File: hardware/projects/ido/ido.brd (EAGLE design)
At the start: 48.3 x 48.3 mm, 36 parts, among them U1 PADI-IOT-STAMP, U2 POLOLU-BUCK, U3 AL8805W5, U4 AL8805W5, U5 AL8805W5, X1 PROGRAMMING-HEADER, X10 WIRE-HOLE, X2 UART-HEADER, X3 WIRE-HOLE, X4 WIRE-HOLE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

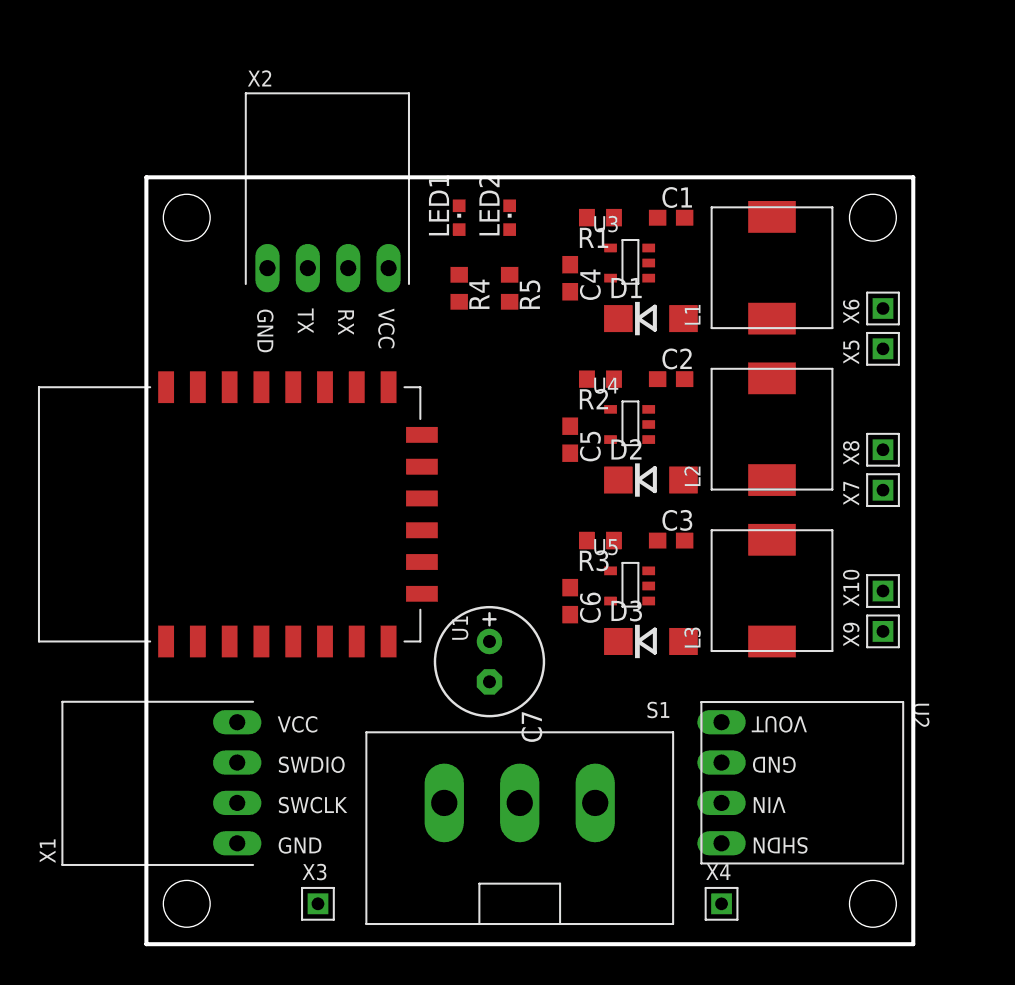
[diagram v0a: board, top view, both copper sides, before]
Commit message: Board and hole dimensions set and layout WIP.
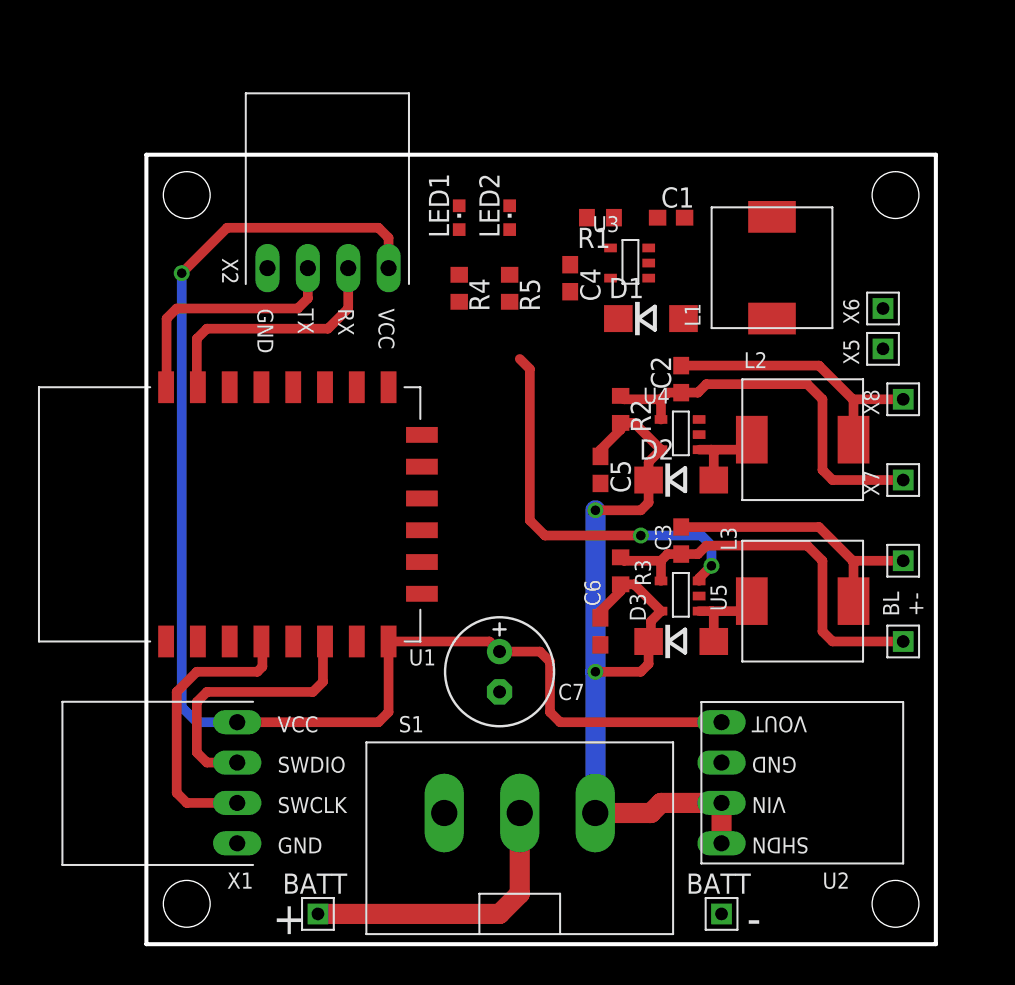
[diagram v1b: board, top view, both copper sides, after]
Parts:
- moved X8 3.42 mm to (47.6, 34.3)
- moved U5 3.24 mm to (32.4, 22.9)
- moved U4 3.24 mm to (32.4, 33.0)
- moved L2 2.84 mm to (38.1, 31.8), turned to 0 degrees
- moved L3 2.84 mm to (38.1, 21.6), turned to 0 degrees
- moved C5 2.69 mm to (28.6, 29.8)
- moved C6 2.69 mm to (28.6, 19.7)
- moved R2 2.29 mm to (29.8, 33.7), turned to 270 degrees
- moved X10 2.29 mm to (47.6, 24.1)
- moved R3 2.29 mm to (29.8, 23.5), turned to 270 degrees
- moved D2 1.91 mm to (33.7, 29.2)
- moved D3 1.91 mm to (33.7, 19.1)
- moved X7 1.42 mm to (47.6, 29.2)
- moved X9 1.42 mm to (47.6, 19.1)
- moved C7 0.90 mm to (22.2, 17.1)
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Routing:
- net +3V3: track 0.00 -> 86.7 mm, vias 0 -> 1
- net V+: track 0.00 -> 56.0 mm, vias 0 -> 2
- net BCTRL: track 0.00 -> 25.1 mm, vias 0 -> 2
- net G+: track 0.00 -> 24.6 mm
- net B+: track 0.00 -> 24.6 mm
- net N$1: track 0.00 -> 18.3 mm
- net SWCLK: track 0.00 -> 18.1 mm
- net B-: track 0.00 -> 17.4 mm
- net G-: track 0.00 -> 17.4 mm
- net SWDIO: track 0.00 -> 17.0 mm
- net RX: track 0.00 -> 15.9 mm
- net TX: track 0.00 -> 15.7 mm
- net N$9: track 0.00 -> 5.55 mm
- net N$6: track 0.00 -> 5.55 mm
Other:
- board size 48.3 x 48.3 mm -> 49.7 x 49.7 mm
- board text added: "+"
- board text added: "-"
- board text added: "BATT"
- board text added: "BL +-"

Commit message: Final board rev.
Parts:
- moved X3 39.8 mm to (49.8, 9.53), turned to 90 degrees
- moved X4 17.8 mm to (49.8, 13.3), turned to 90 degrees
- moved LED2 14.0 mm to (21.6, 31.8), turned to 270 degrees
- moved R5 12.8 mm to (21.6, 28.6), turned to 0 degrees
- moved X2 12.7 mm to (19.7, 46.4)
- moved LED1 8.16 mm to (21.6, 37.8), turned to 270 degrees
- moved R4 6.93 mm to (21.6, 34.6), turned to 0 degrees
- moved U1 5.71 mm to (15.2, 24.8)
- moved U2 5.68 mm to (41.3, 11.4), turned to 180 degrees
- moved U3 5.12 mm to (33.7, 41.3)
- moved C4 4.96 mm to (29.8, 38.1)
- moved R1 4.58 mm to (31.1, 41.9), turned to 270 degrees
- moved X1 4.45 mm to (5.71, 10.8)
- moved X6 3.98 mm to (49.8, 41.9)
- moved D1 3.70 mm to (34.9, 37.5)
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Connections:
- removed net N$2: LED1.A, R4.1
- new net N$5: LED1.C, R4.2
- net DEBUG1: now also LED1.A; no longer R4.2
- net DEBUG2: now also LED2.A; no longer R5.2
- net GND: now also R4.1, R5.1; no longer LED1.C, LED2.C
- net N$3: now also LED2.C, R5.2; no longer LED2.A, R5.1
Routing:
- net RCTRL: track 0.00 -> 42.5 mm, vias 0 -> 2
- net GCTRL: track 0.00 -> 42.2 mm, vias 0 -> 2
- net R+: track 0.00 -> 25.9 mm
- net V+: track 56.0 -> 80.4 mm, vias 2 -> 3
- net BCTRL: track 25.1 -> 47.9 mm
- net R-: track 0.00 -> 18.4 mm
- net N$1: track 18.3 -> 34.8 mm
- net +3V3: track 86.7 -> 102.1 mm, vias 1 -> 0
- net RX: track 15.9 -> 27.3 mm
- net TX: track 15.7 -> 26.8 mm
- net N$4: track 0.00 -> 5.55 mm
- net DEBUG1: track 0.00 -> 3.51 mm
- net DEBUG2: track 0.00 -> 3.51 mm
- net N$3: track 0.00 -> 3.22 mm
- net N$5: track 0.00 -> 3.22 mm
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- added copper zone on layer 1, net GND
- added copper zone on layer 16, net GND
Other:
- board size 49.7 x 49.7 mm -> 52.5 x 52.5 mm
- board text added: "2017-05-19"
- board text added: "BAT"
- board text added: "BLU"
- board text added: "GRN"
- board text added: "Maria & Bob"
- board text added: "RED"
- board text added: "iDo v1.0"
- board text removed: "BATT"
- board text removed: "BL +-"

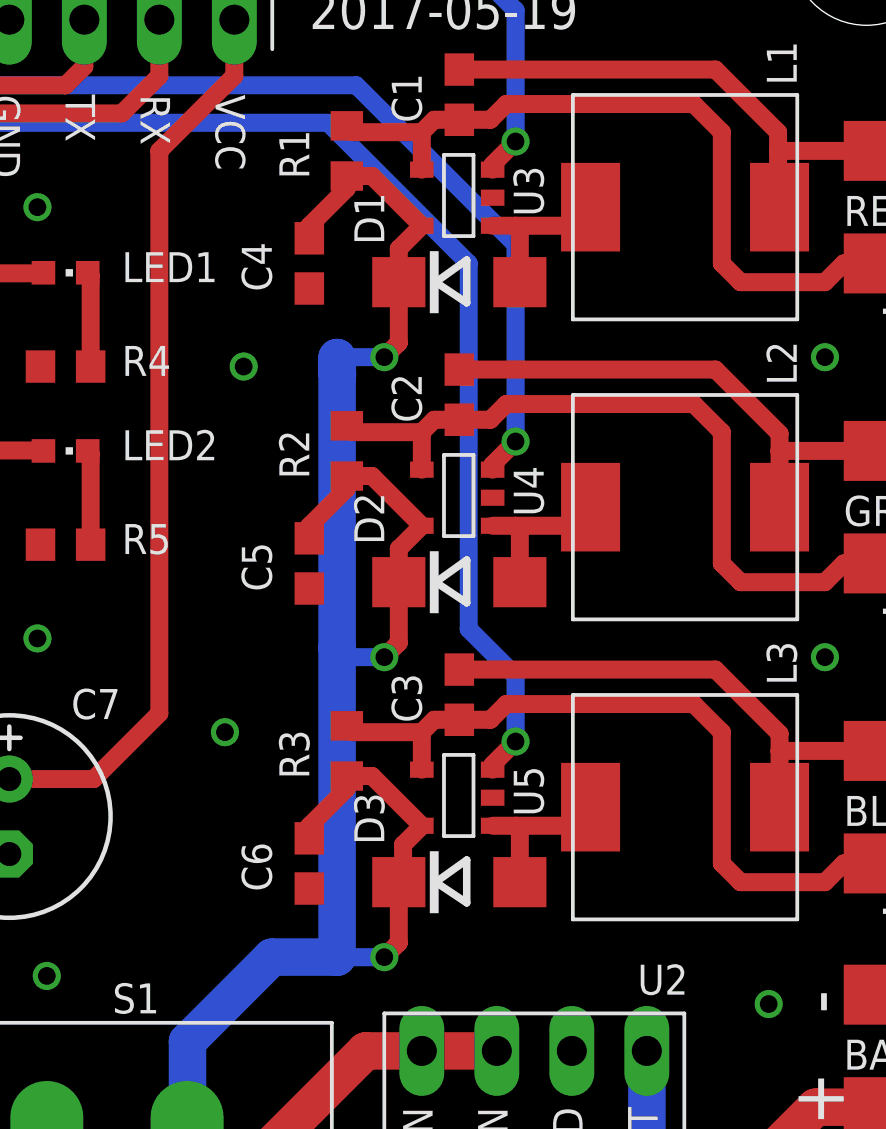
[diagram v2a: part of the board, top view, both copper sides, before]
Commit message: Move diodes down a bit to make assembly easier.
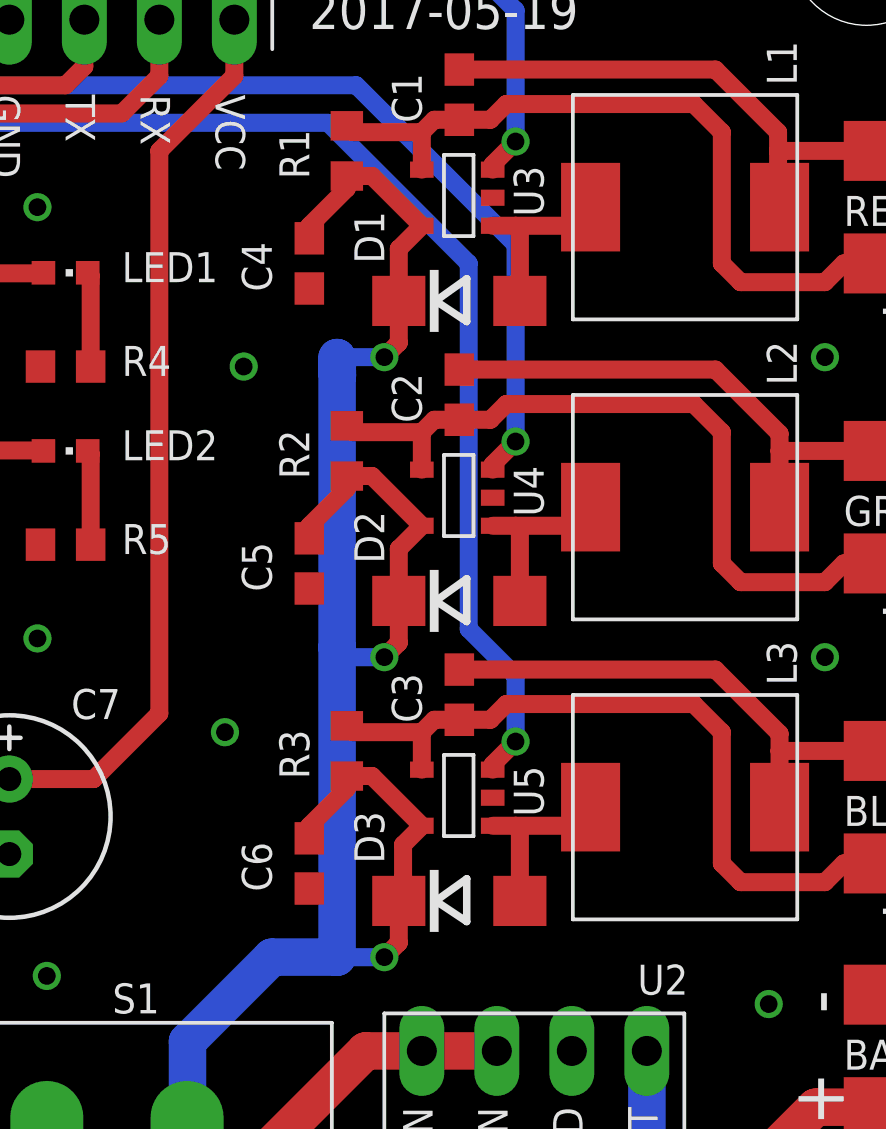
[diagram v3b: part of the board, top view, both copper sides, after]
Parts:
- moved D1 0.64 mm to (34.9, 36.8)
- moved D2 0.63 mm to (34.9, 26.7)
- moved D3 0.63 mm to (34.9, 16.5)
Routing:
- net N$4: track 5.55 -> 6.18 mm
- net N$9: track 5.55 -> 6.18 mm
- net N$6: track 5.55 -> 6.18 mm
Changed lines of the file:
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@@
 <attribute name="VALUE" x="16.51" y="16.3195" size="1.27" layer="27" ratio="10" rot="R270"/>
 </element>
-<element name="D1" library="diode" package="DO214AC" value="" x="34.925" y="37.465" smashed="yes">
-<attribute name="NAME" x="32.385" y="38.735" size="1.016" layer="25" font="vector" ratio="15" rot="R90"/>
-<attribute name="VALUE" x="32.285" y="34.909" size="1.27" layer="27" ratio="10"/>
-</element>
-<element name="D2" library="diode" package="DO214AC" value="" x="34.925" y="27.305" smashed="yes">
-<attribute name="NAME" x="32.385" y="28.575" size="1.016" layer="25" font="vector" ratio="15" rot="R90"/>
-<attribute name="VALUE" x="32.285" y="24.749" size="1.27" layer="27" ratio="10"/>
-</element>
-<element name="D3" library="diode" package="DO214AC" value="" x="34.925" y="17.145" smashed="yes">
-<attribute name="NAME" x="32.385" y="18.415" size="1.016" layer="25" font="vector" ratio="15" rot="R90"/>
-<attribute name="VALUE" x="32.285" y="14.589" size="1.27" layer="27" ratio="10"/>
+<element name="D1" library="diode" package="DO214AC" value="" x="34.925" y="36.83" smashed="yes">
+<attribute name="NAME" x="32.385" y="38.1" size="1.016" layer="25" font="vector" ratio="15" rot="R90"/>
+<attribute name="VALUE" x="32.285" y="34.274" size="1.27" layer="27" ratio="10"/>
+</element>
+<element name="D2" library="diode" package="DO214AC" value="" x="34.925" y="26.67" smashed="yes">
+<attribute name="NAME" x="32.385" y="27.94" size="1.016" layer="25" font="vector" ratio="15" rot="R90"/>
+<attribute name="VALUE" x="32.285" y="24.114" size="1.27" layer="27" ratio="10"/>
+</element>
+<element name="D3" library="diode" package="DO214AC" value="" x="34.925" y="16.51" smashed="yes">
+<attribute name="NAME" x="32.385" y="17.78" size="1.016" layer="25" font="vector" ratio="15" rot="R90"/>
+<attribute name="VALUE" x="32.285" y="13.954" size="1.27" layer="27" ratio="10"/>
 </element>
 <element name="L1" library="ido" package="MURATA-INDUCTOR" value="33uH" x="39.37" y="40.005" smashed="yes">
@@
 <wire x1="33.655" y1="19.05" x2="33.02" y2="18.415" width="0.6096" layer="1"/>
 <wire x1="33.02" y1="18.415" x2="33.02" y2="17.29" width="0.6096" layer="1"/>
-<wire x1="33.02" y1="17.29" x2="32.875" y2="17.145" width="0.6096" layer="1"/>
+<wire x1="33.02" y1="17.29" x2="32.875" y2="16.51" width="0.6096" layer="1"/>
 <wire x1="31.115" y1="20.74" x2="31.97" y2="20.74" width="0.6096" layer="1"/>
 <wire x1="31.97" y1="20.74" x2="33.655" y2="19.055" width="0.6096" layer="1"/>
@@
 <wire x1="31.115" y1="30.9" x2="31.97" y2="30.9" width="0.6096" layer="1"/>
 <wire x1="31.97" y1="30.9" x2="33.655" y2="29.215" width="0.6096" layer="1"/>
-<wire x1="32.875" y1="27.305" x2="32.875" y2="28.435" width="0.6096" layer="1"/>
+<wire x1="32.875" y1="26.67" x2="32.875" y2="28.435" width="0.6096" layer="1"/>
 <wire x1="32.875" y1="28.435" x2="33.655" y2="29.215" width="0.6096" layer="1"/>
 <wire x1="29.845" y1="28.79" x2="29.845" y2="29.21" width="0.6096" layer="1"/>
@@
 <wire x1="31.115" y1="41.06" x2="31.97" y2="41.06" width="0.6096" layer="1"/>
 <wire x1="31.97" y1="41.06" x2="33.655" y2="39.375" width="0.6096" layer="1"/>
-<wire x1="32.875" y1="37.465" x2="32.875" y2="38.595" width="0.6096" layer="1"/>
+<wire x1="32.875" y1="36.83" x2="32.875" y2="38.595" width="0.6096" layer="1"/>
 <wire x1="32.875" y1="38.595" x2="33.655" y2="39.375" width="0.6096" layer="1"/>
 <wire x1="29.845" y1="38.95" x2="29.845" y2="39.37" width="0.6096" layer="1"/>
@@
 <wire x1="30.7848" y1="14.605" x2="30.7848" y2="25.0952" width="1.27" layer="16"/>
 <wire x1="33.655" y1="11.43" x2="36.195" y2="11.43" width="1.27" layer="1"/>
-<wire x1="32.875" y1="17.145" x2="32.875" y2="15.095" width="0.6096" layer="1"/>
+<wire x1="32.875" y1="16.51" x2="32.875" y2="15.095" width="0.6096" layer="1"/>
 <wire x1="32.875" y1="15.095" x2="32.385" y2="14.605" width="0.6096" layer="1"/>
 <via x="32.385" y="14.605" extent="1-16" drill="0.6"/>
 <wire x1="32.385" y1="14.605" x2="30.7848" y2="14.605" width="0.6096" layer="16"/>
 <wire x1="30.7848" y1="25.0952" x2="31.115" y2="24.765" width="0.6096" layer="16"/>
-<wire x1="32.875" y1="27.305" x2="32.875" y2="25.255" width="0.6096" layer="1"/>
+<wire x1="32.875" y1="26.67" x2="32.875" y2="25.255" width="0.6096" layer="1"/>
 <wire x1="32.875" y1="25.255" x2="32.385" y2="24.765" width="0.6096" layer="1"/>
 <via x="32.385" y="24.765" extent="1-16" drill="0.6"/>
 <wire x1="32.385" y1="24.765" x2="31.115" y2="24.765" width="0.6096" layer="16"/>
-<wire x1="32.875" y1="37.465" x2="32.875" y2="35.415" width="0.6096" layer="1"/>
+<wire x1="32.875" y1="36.83" x2="32.875" y2="35.415" width="0.6096" layer="1"/>
 <wire x1="32.875" y1="35.415" x2="32.385" y2="34.925" width="0.6096" layer="1"/>
 <via x="32.385" y="34.925" extent="1-16" drill="0.6"/>
@@
 <wire x1="36.83" y1="39.375" x2="38.74" y2="39.375" width="0.6096" layer="1"/>
 <wire x1="38.74" y1="39.375" x2="39.37" y2="40.005" width="0.6096" layer="1"/>
-<wire x1="36.975" y1="37.465" x2="36.975" y2="39.23" width="0.6096" layer="1"/>
+<wire x1="36.975" y1="36.83" x2="36.975" y2="39.23" width="0.6096" layer="1"/>
 <wire x1="36.975" y1="39.23" x2="36.83" y2="39.375" width="0.6096" layer="1"/>
 </signal>
@@
 <wire x1="36.83" y1="29.215" x2="38.74" y2="29.215" width="0.6096" layer="1"/>
 <wire x1="38.74" y1="29.215" x2="39.37" y2="29.845" width="0.6096" layer="1"/>
-<wire x1="36.975" y1="27.305" x2="36.975" y2="29.07" width="0.6096" layer="1"/>
+<wire x1="36.975" y1="26.67" x2="36.975" y2="29.07" width="0.6096" layer="1"/>
 <wire x1="36.975" y1="29.07" x2="36.83" y2="29.215" width="0.6096" layer="1"/>
 </signal>
@@
 <wire x1="38.74" y1="19.055" x2="36.83" y2="19.055" width="0.6096" layer="1"/>
 <wire x1="36.83" y1="19.055" x2="36.055" y2="19.055" width="0.6096" layer="1"/>
-<wire x1="36.975" y1="17.145" x2="36.975" y2="18.91" width="0.6096" layer="1"/>
+<wire x1="36.975" y1="16.51" x2="36.975" y2="18.91" width="0.6096" layer="1"/>
 <wire x1="36.975" y1="18.91" x2="36.83" y2="19.055" width="0.6096" layer="1"/>
 </signal>
